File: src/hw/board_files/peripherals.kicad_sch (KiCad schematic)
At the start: 7 parts, among them J1 MSD-1-A, U4 NEO-M9N, U6 SHT30-DIS

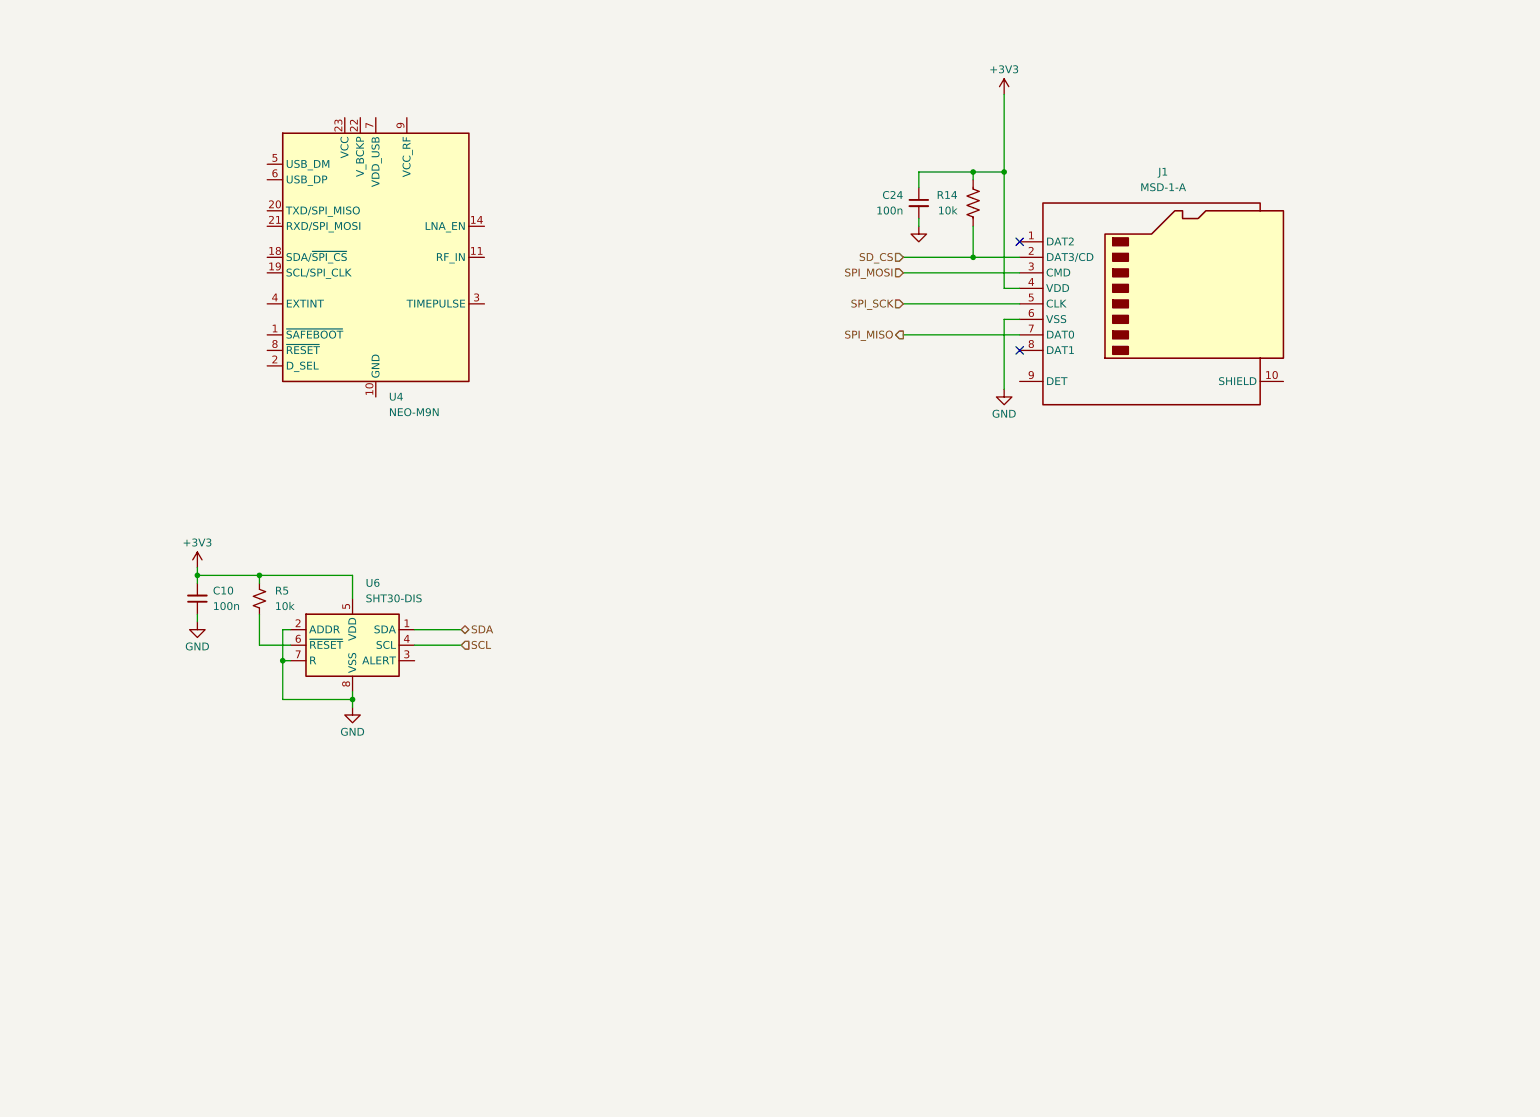
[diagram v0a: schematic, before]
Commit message: Schematic updates
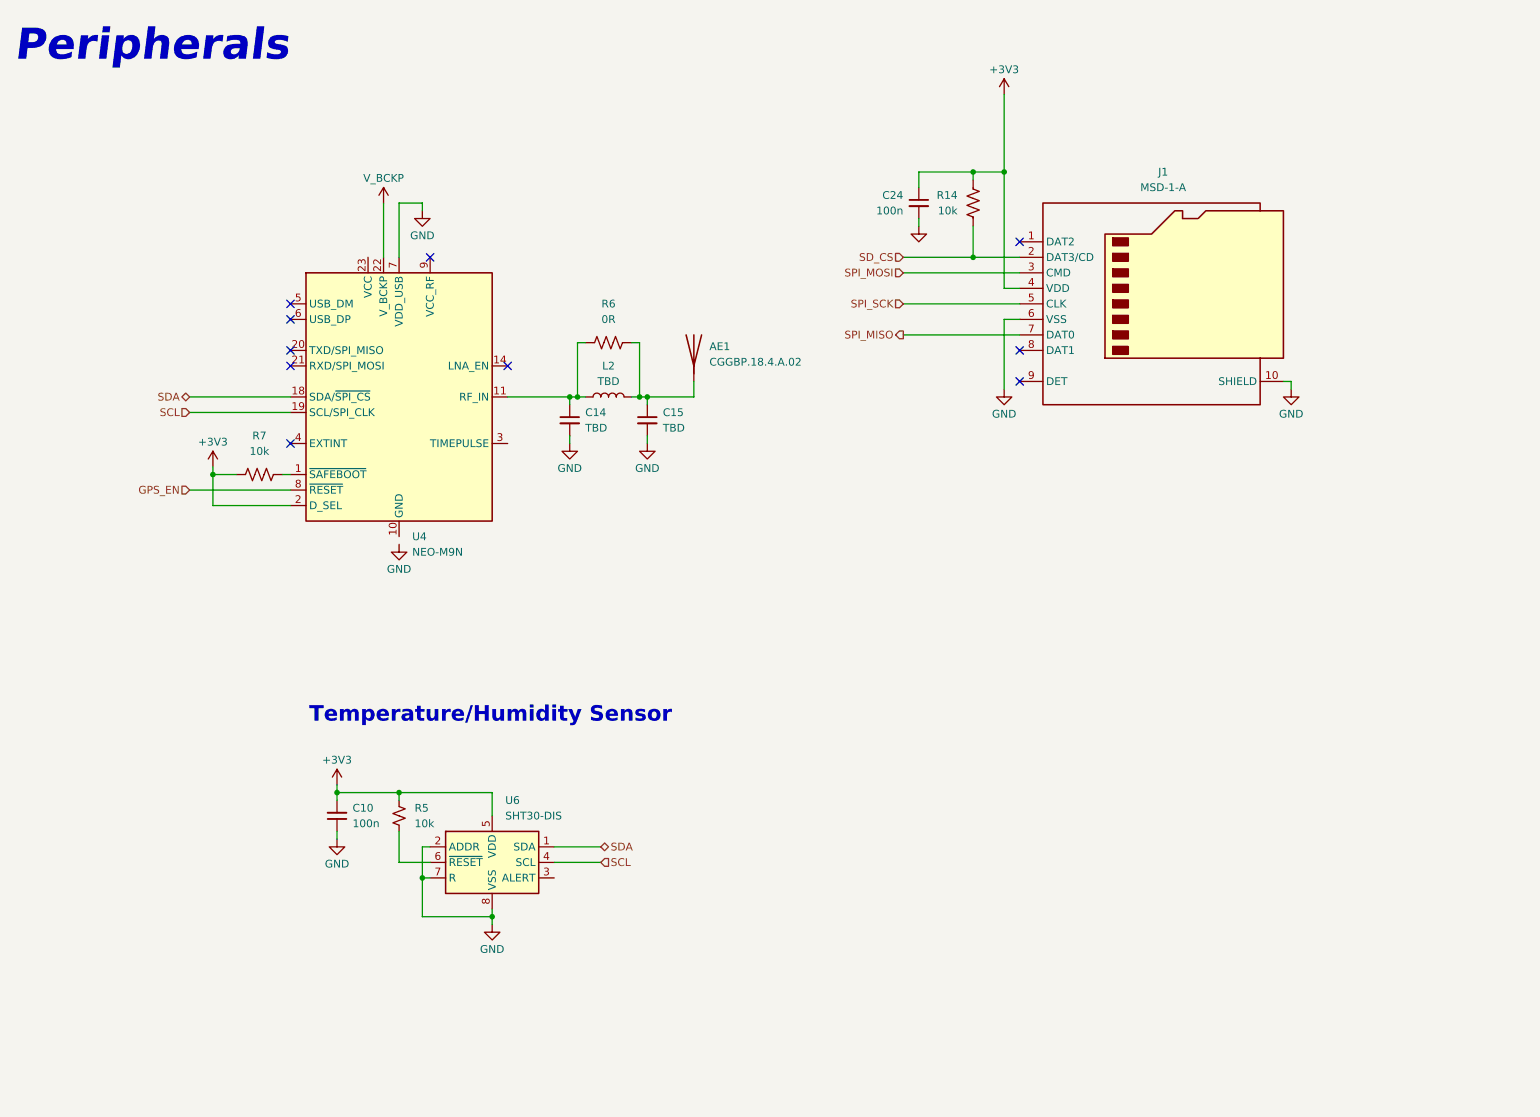
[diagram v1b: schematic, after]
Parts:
- added AE1: CGGBP.18.4.A.02, symbol Device:Antenna
- added C14, C15: TBD, symbol Device:C_Small
- added L2: TBD, symbol Device:L
- added R6: 0R, symbol Device:R_US
- added R7: 10k, symbol Device:R_US
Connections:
- net +3V3: now also U4.2 (D_SEL), R7.1
- net GND: now also J1.10 (SHIELD), U4.7 (VDD_USB), C14.2, C15.2
- net SCL: now also U4.19 (SCL/SPI_CLK)
- net SDA: now also U4.18 (SDA/~{SPI_CS})
- net at U4.1 (~{SAFEBOOT}): now also R7.2
- net at U4.11 (RF_IN): now also C14.1, L2.1, R6.1
- net V_BCKP: now reaches U4.22 (V_BCKP)
- net GPS_EN: now reaches U4.8 (~{RESET})
- new net: AE1.1 (A), C15.1, L2.2, R6.2
- no-connect marks 2 -> 10
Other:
- note added: "Peripherals"
- note added: "Temperature/Humidity Sensor"
- company: (none) -> EE 333 - Electronic Systems Design
- title: (none) -> Pocket Caddy
- moved on the sheet: C10, R5, U4, U6

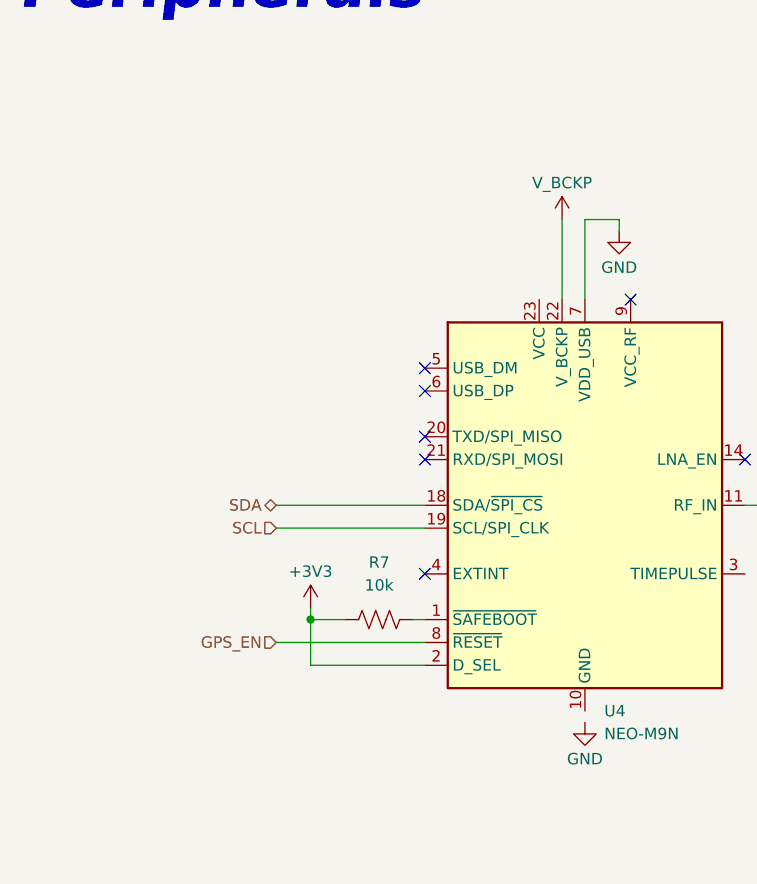
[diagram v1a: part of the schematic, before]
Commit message: Put USB to UART bridge back and added jumpers to USB lines
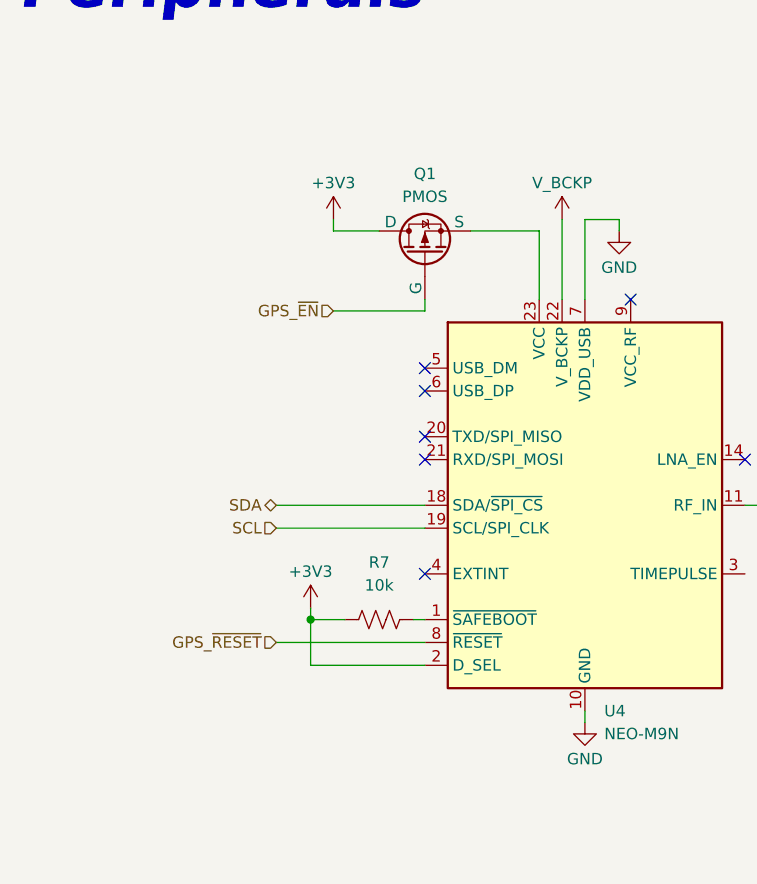
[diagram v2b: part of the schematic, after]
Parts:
- added Q1: PMOS, symbol Simulation_SPICE:PMOS
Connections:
- net +3V3: now also Q1.1 (D)
- net GND: now also U4.10 (GND), U4.12 (GND), U4.13 (GND), U4.24 (GND)
- net at U4.23 (VCC): now also Q1.3 (S)
- net GPS_EN renamed GPS_~{RESET}
- new net GPS_~{EN}: Q1.2 (G)
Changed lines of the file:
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@@
+	(wire
+		(pts
+			(xy 49.53 44.45) (xy 49.53 45.72)
+		)
+		(stroke
+			(width 0)
+			(type default)
+		)
+	)
 	(wire
 		(pts
@@
 	(wire
 		(pts
+			(xy 77.47 99.06) (xy 77.47 100.33)
+		)
+		(stroke
+			(width 0)
+			(type default)
+		)
+	)
+	(wire
+		(pts
 			(xy 92.71 161.29) (xy 92.71 162.56)
 		)
@@
 	(wire
 		(pts
+			(xy 72.39 45.72) (xy 64.77 45.72)
+		)
+		(stroke
+			(width 0)
+			(type default)
+		)
+	)
+	(wire
+		(pts
 			(xy 102.87 149.86) (xy 110.49 149.86)
 		)
@@
 	(wire
 		(pts
+			(xy 49.53 54.61) (xy 59.69 54.61)
+		)
+		(stroke
+			(width 0)
+			(type default)
+		)
+	)
+	(wire
+		(pts
 			(xy 223.52 73.66) (xy 223.52 74.93)
 		)
@@
 	(wire
 		(pts
+			(xy 72.39 45.72) (xy 72.39 53.34)
+		)
+		(stroke
+			(width 0)
+			(type default)
+		)
+	)
+	(wire
+		(pts
 			(xy 92.71 144.78) (xy 92.71 140.97)
 		)
@@
 	(wire
 		(pts
+			(xy 59.69 54.61) (xy 59.69 53.34)
+		)
+		(stroke
+			(width 0)
+			(type default)
+		)
+	)
+	(wire
+		(pts
 			(xy 160.02 55.88) (xy 179.07 55.88)
 		)
@@
 	(wire
 		(pts
+			(xy 49.53 45.72) (xy 54.61 45.72)
+		)
+		(stroke
+			(width 0)
+			(type default)
+		)
+	)
+	(wire
+		(pts
 			(xy 46.99 93.98) (xy 46.99 88.9)
 		)
@@
 		)
 	)
-	(hierarchical_label "GPS_EN"
+	(hierarchical_label "GPS_~{RESET}"
 		(shape input)
 		(at 43.18 91.44 180)
@@
 				(size 1.27 1.27)
 				(thickness 0.1588)
+			)
+			(justify right)
+		)
+	)
+	(hierarchical_label "GPS_~{EN}"
+		(shape input)
+		(at 49.53 54.61 180)
+		(effects
+			(font
+				(size 1.27 1.27)
 			)
 			(justify right)
@@
 	)
 	(symbol
+		(lib_id "power:+3V3")
+		(at 49.53 44.45 0)
+		(unit 1)
+		(exclude_from_sim no)
+		(in_bom yes)
+		(on_board yes)
+		(dnp no)
+		(property "Reference" "#PWR043"
+			(at 49.53 48.26 0)
+			(effects
+				(font
+					(size 1.27 1.27)
+				)
+				(hide yes)
+			)
+		)
+		(property "Value" "+3V3"
+			(at 49.53 40.386 0)
+			(effects
+				(font
+					(size 1.27 1.27)
+				)
+			)
+		)
+		(property "Footprint" ""
+			(at 49.53 44.45 0)
+			(effects
+				(font
+					(size 1.27 1.27)
+				)
+				(hide yes)
+			)
+		)
+		(property "Datasheet" ""
+			(at 49.53 44.45 0)
+			(effects
+				(font
+					(size 1.27 1.27)
+				)
+				(hide yes)
+			)
+		)
+		(property "Description" "Power symbol creates a global label with name \"+3V3\""
+			(at 49.53 44.45 0)
+			(effects
+				(font
+					(size 1.27 1.27)
+				)
+				(hide yes)
+			)
+		)
+		(pin "1"
+		)
+		(instances
+			(project "pocket-caddy"
+				(path "/2c77a8ba-b277-4959-adec-d3fc778c7960/81382524-b053-4c3c-9e13-c8b314c52639"
+					(reference "#PWR043")
+					(unit 1)
+				)
+			)
+		)
+	)
+	(symbol
 		(lib_id "Device:R_US")
 		(at 111.76 67.31 90)
@@
 					(unit 1)
 				)
+			)
+		)
+	)
+	(symbol
+		(lib_id "Simulation_SPICE:PMOS")
+		(at 59.69 48.26 90)
+		(unit 1)
+		(exclude_from_sim no)
+		(in_bom yes)
+		(on_board yes)
+		(dnp no)
+		(fields_autoplaced yes)
+		(property "Reference" "Q1"
+			(at 59.69 39.37 90)
+			(effects
+				(font
+					(size 1.27 1.27)
+				)
+			)
+		)
+		(property "Value" "PMOS"
+			(at 59.69 41.91 90)
+			(effects
+				(font
+					(size 1.27 1.27)
+				)
+			)
+		)
+		(property "Footprint" ""
+			(at 57.15 43.18 0)
+			(effects
+				(font
+					(size 1.27 1.27)
+				)
+				(hide yes)
+			)
+		)
+		(property "Datasheet" "https://ngspice.sourceforge.io/docs/ngspice-html-manual/manual.xhtml#cha_MOSFETs"
+			(at 72.39 48.26 0)
+			(effects
+				(font
+					(size 1.27 1.27)
+				)
+				(hide yes)
+			)
+		)
+		(property "Description" "P-MOSFET transistor, drain/source/gate"
+			(at 59.69 48.26 0)
+			(effects
+				(font
+					(size 1.27 1.27)
+				)
+				(hide yes)
+			)
+		)
+		(property "Sim.Device" "PMOS"
+			(at 76.835 48.26 0)
+			(effects
+				(font
+					(size 1.27 1.27)
+				)
+				(hide yes)
+			)
+		)
+		(property "Sim.Type" "VDMOS"
+			(at 78.74 48.26 0)
+			(effects
+				(font
+					(size 1.27 1.27)
+				)
+				(hide yes)
+			)
+		)
+		(property "Sim.Pins" "1=D 2=G 3=S"
+			(at 74.93 48.26 0)
+			(effects
+				(font
+					(size 1.27 1.27)
+				)
+				(hide yes)
+			)
+		)
+		(pin "3"
+		)
+		(pin "1"
+		)
+		(pin "2"
+		)
+		(instances
+			(project ""
+				(path "/2c77a8ba-b277-4959-adec-d3fc778c7960/81382524-b053-4c3c-9e13-c8b314c52639"
+					(reference "Q1")
+					(unit 1)
+				)
